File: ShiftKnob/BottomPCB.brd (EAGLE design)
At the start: 38.1 x 38.1 mm, 38 parts, among them IC2 UA78M05DCY, J1 AVR_SPI_PRG_6PTH, Q1 16MHz, Q2 MOSFET-NCHANNELSMD, Q3 MOSFET-PCHANNELSMD, Q4 MOSFET-NCHANNELSMD, Q5 MOSFET-NCHANNELSMD, Q6 MOSFET-NCHANNELSMD, U1 ATMEGA328, U3 FT232RL-BASICSSOP

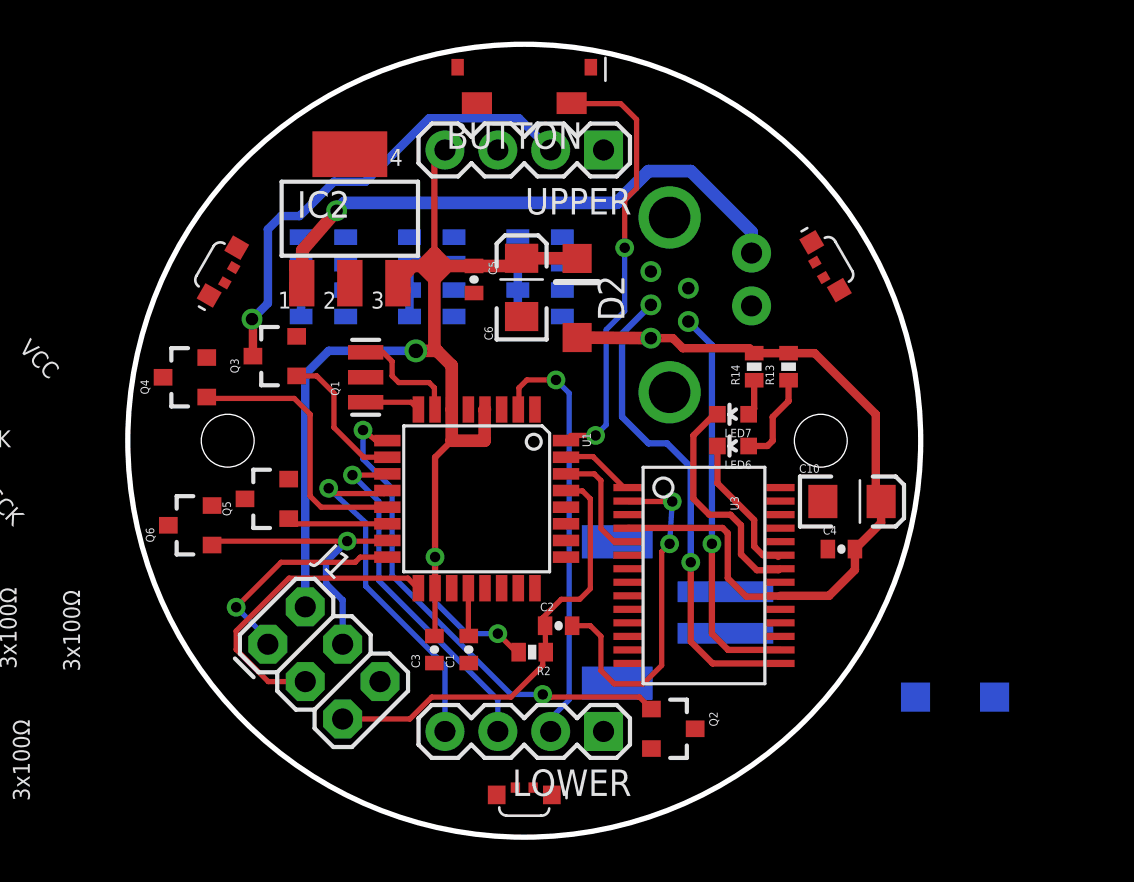
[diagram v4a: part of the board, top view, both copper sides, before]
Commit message: board layout done. DRC check complete and all errors fixed. Only silk screens remaining.
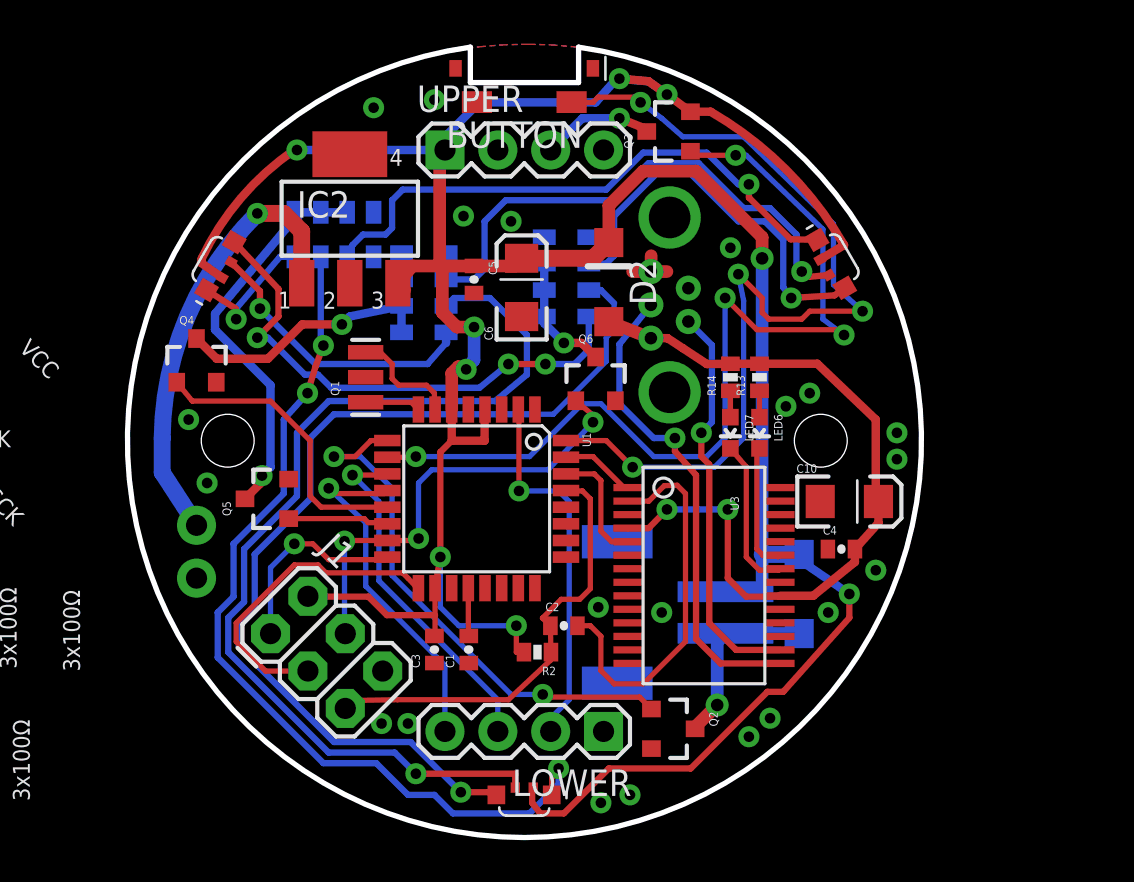
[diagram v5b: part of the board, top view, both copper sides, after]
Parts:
- moved U$3 59.7 mm to (21.4, 16.8), turned to 0 degrees
- moved JP3 29.7 mm to (5.84, 17.5)
- moved LED1 29.5 mm to (36.3, 30.1), turned to 300 degrees
- moved LED2 29.2 mm to (21.6, 4.57), turned to 180 degrees
- moved Q3 21.8 mm to (28.6, 36.4)
- moved Q6 20.6 mm to (25.0, 24.5), turned to 0 degrees
- moved D1 8.98 mm to (34.8, 14.2), turned to 270 degrees
- moved UPPER 7.62 mm to (17.8, 35.6), turned to 0 degrees
- moved RN3 2.09 mm to (12.4, 31.5), turned to 180 degrees
- moved D2 1.70 mm to (25.7, 29.2)
- moved R13 1.49 mm to (32.9, 24.6)
- moved LED6 1.42 mm to (32.9, 22.0), turned to 180 degrees
- moved RN2 1.27 mm to (23.6, 29.5)
- moved R14 1.25 mm to (31.5, 24.6)
- moved Q4 0.92 mm to (5.84, 25.4), turned to 0 degrees
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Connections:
- removed net N$25: LED2.1, RN3.8
- new net N$20: LED3.1, RN3.8
- net GND: now also UPPER.2, UPPER.4; no longer UPPER.1, UPPER.3
- net INPUT+: now also UPPER.3; no longer UPPER.2
- net MOTOR-: now also JP4.2; no longer JP4.1
- net N$16: now also LED2.1; no longer LED3.1
- net N$4: now also RN1.7; no longer RN1.8
- net N$5: now also RN2.7; no longer RN2.8
- net N$6: now also RN1.8; no longer RN1.7
- net N$8: now also RN2.8; no longer RN2.7
- net VCC: now also JP4.1, UPPER.1; no longer JP4.2, UPPER.4
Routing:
- net VCC: track 64.7 -> 156.4 mm, vias 3 -> 9
- net N$4: track 0.00 -> 47.6 mm, vias 0 -> 1
- net N$5: track 0.00 -> 46.9 mm, vias 0 -> 1
- net N$16: track 0.00 -> 43.5 mm, vias 0 -> 3
- net D6/INPUT+: track 6.95 -> 45.3 mm, vias 0 -> 4
- net N$7: track 0.00 -> 27.7 mm, vias 0 -> 1
- net N$9: track 0.00 -> 25.7 mm, vias 0 -> 1
- net N$8: track 0.00 -> 25.1 mm, vias 0 -> 3
- net D2: track 20.9 -> 44.9 mm, vias 2 -> 4
- net N$10: track 0.00 -> 19.2 mm, vias 0 -> 1
- net INPUT+: track 22.9 -> 5.44 mm
- net D10: track 2.54 -> 19.3 mm, vias 0 -> 1
- net N$6: track 0.00 -> 13.8 mm, vias 0 -> 1
- net D9: track 2.54 -> 13.7 mm, vias 0 -> 1
- net MOTOR-: track 0.00 -> 8.73 mm, vias 0 -> 1
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- added copper zone on layer 1, net GND
- added copper zone on layer 16, net GND
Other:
- board size 38.1 x 38.1 mm -> 38.1 x 38 mm
- board text added: "4.05.13"
- board text removed: "2-07-13"

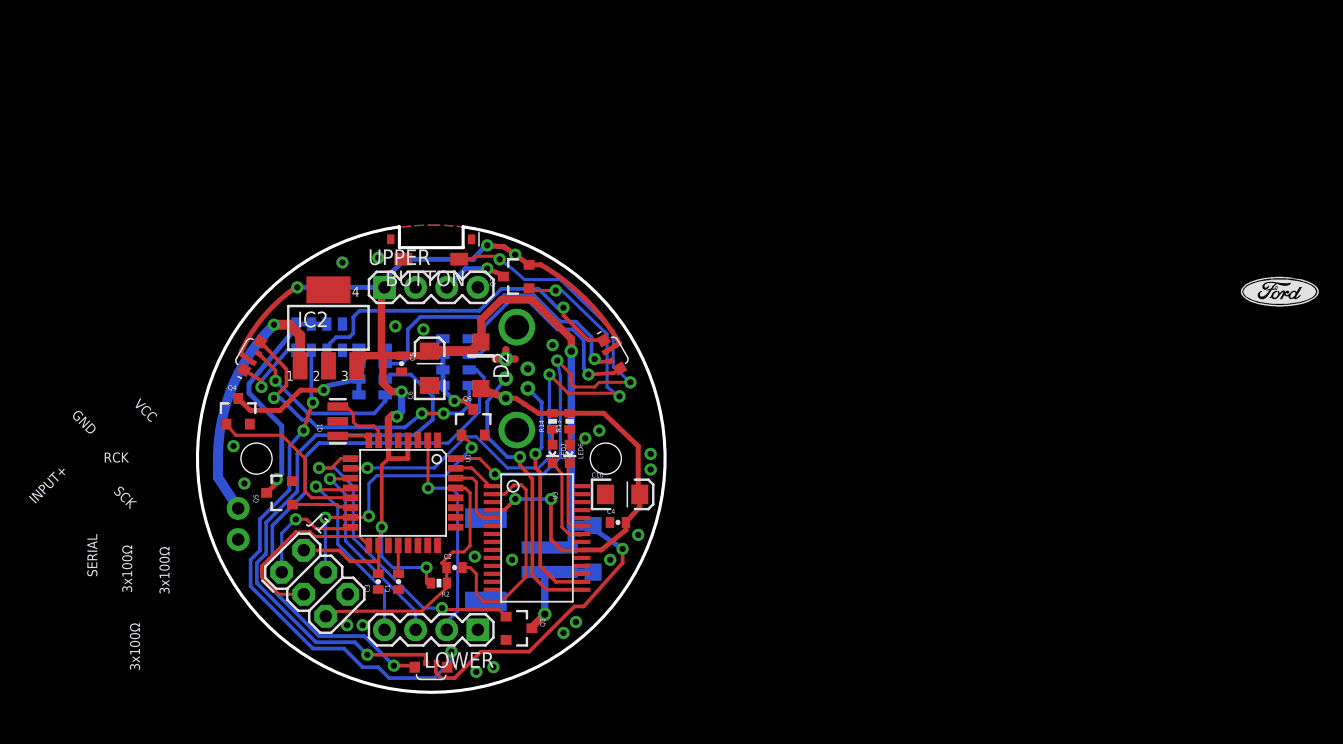
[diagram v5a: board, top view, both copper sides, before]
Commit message: Bottom board layout is finalized. 1st attempt at generating gerber files failed BatchPCB test.
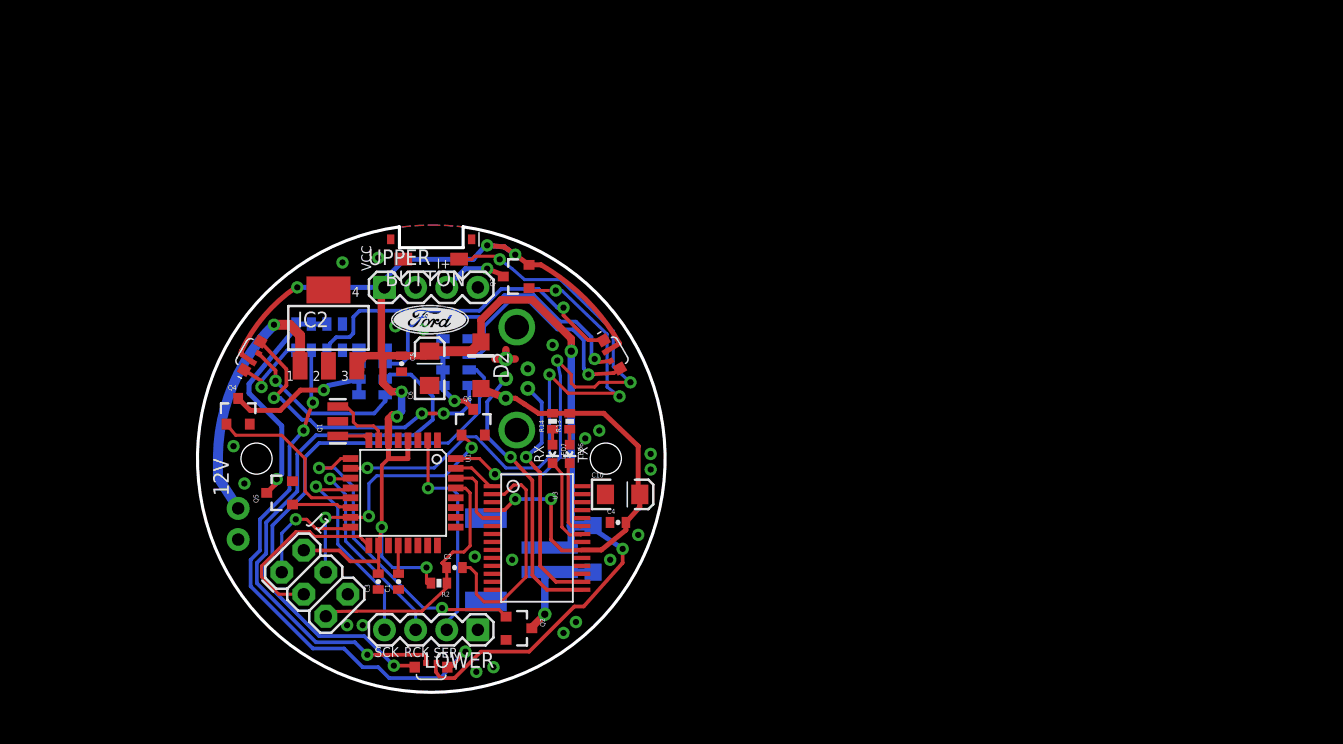
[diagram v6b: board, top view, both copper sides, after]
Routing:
- net N$16: track 43.5 -> 44.9 mm
- net N$22: track 19.3 -> 19.9 mm
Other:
- board text added: "100Ω"
- board text added: "12V"
- board text added: "150Ω"
- board text added: "I+"
- board text added: "RX"
- board text added: "SER"
- board text added: "TX"
- board text removed: "3x100Ω"
- board text removed: "GND"
- board text removed: "INPUT+"
- board text removed: "SERIAL"
